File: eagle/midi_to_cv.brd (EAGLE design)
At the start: 100 x 80 mm, 57 parts, among them IC1 TL084P, IC2 TL084P, U1 ATMEGA328P_PDIP

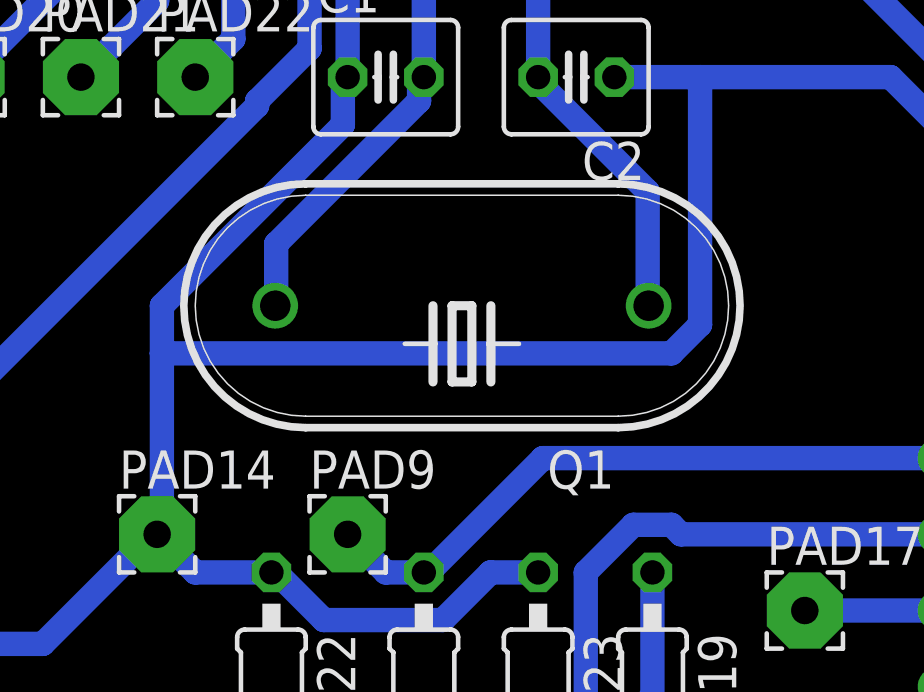
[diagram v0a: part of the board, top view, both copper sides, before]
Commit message: corrected to smaller xtal package
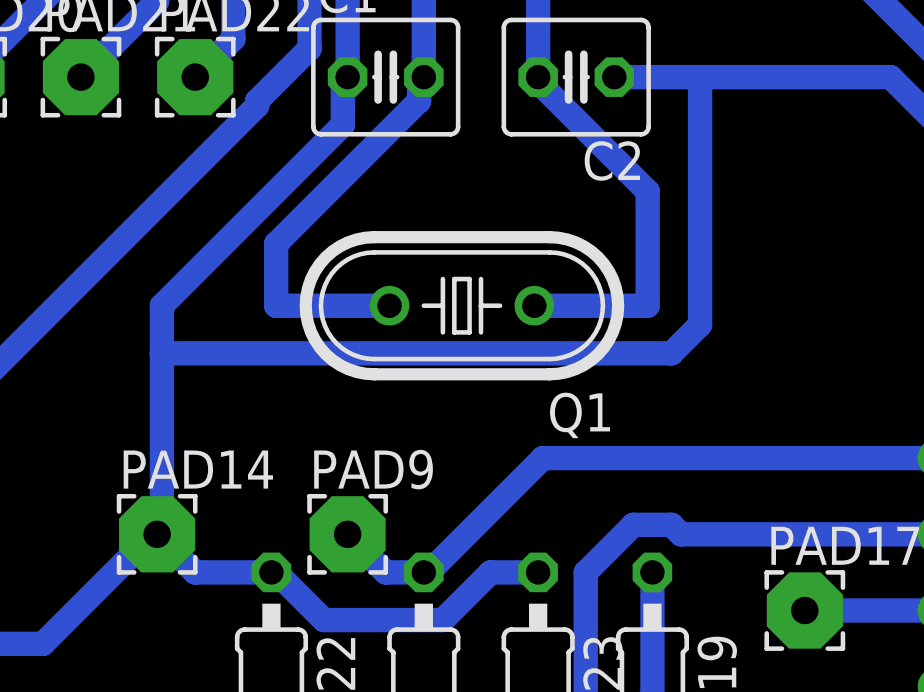
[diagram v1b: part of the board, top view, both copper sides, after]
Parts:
- Q1: device crystal:HC33U-V -> crystal:HC49U-V
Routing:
- net N$4: track 15.3 -> 19.0 mm
- net N$5: track 14.2 -> 18.0 mm
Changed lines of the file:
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@@
 <element name="C1" library="rcl" package="C025-040X050" value="27pF" x="38.1" y="38.1"/>
 <element name="C2" library="rcl" package="C025-040X050" value="27pF" x="44.45" y="38.1" rot="R180"/>
-<element name="Q1" library="crystal" package="HC33U-V" value="" x="40.64" y="30.48" rot="R180">
+<element name="Q1" library="crystal" package="HC49U-V" value="" x="40.64" y="30.48" rot="R180">
 <attribute name="OC_NEWARK" value="unknown" x="40.64" y="30.48" size="1.778" layer="27" rot="R180" display="off"/>
 <attribute name="MPN" value="" x="40.64" y="30.48" size="1.778" layer="27" rot="R180" display="off"/>
 <attribute name="MF" value="" x="40.64" y="30.48" size="1.778" layer="27" rot="R180" display="off"/>
-<attribute name="OC_FARNELL" value="unknown" x="40.64" y="30.48" size="1.778" layer="27" rot="R180" display="off"/>
+<attribute name="OC_FARNELL" value="1666969" x="40.64" y="30.48" size="1.778" layer="27" rot="R180" display="off"/>
 </element>
 <element name="U$1" library="eurorack" package="POWER_16" value="POWER" x="15.24" y="17.78" rot="R90"/>
@@
 <wire x1="39.21125" y1="37.30625" x2="34.44875" y2="32.54375" width="0.8128" layer="16"/>
 <wire x1="39.21125" y1="37.7825" x2="39.21125" y2="37.30625" width="0.8128" layer="16"/>
-<wire x1="34.44875" y1="30.48" x2="34.417" y2="30.48" width="0.8128" layer="16"/>
+<wire x1="34.44875" y1="30.48" x2="38.227" y2="30.48" width="0.8128" layer="16"/>
 <wire x1="39.21125" y1="37.7825" x2="39.37" y2="38.1" width="0.8128" layer="16"/>
 </signal>
@@
 <wire x1="46.83125" y1="34.29" x2="46.83125" y2="30.48" width="0.8128" layer="16"/>
 <wire x1="43.33875" y1="37.7825" x2="46.83125" y2="34.29" width="0.8128" layer="16"/>
-<wire x1="46.83125" y1="30.48" x2="46.863" y2="30.48" width="0.8128" layer="16"/>
+<wire x1="46.83125" y1="30.48" x2="43.053" y2="30.48" width="0.8128" layer="16"/>
 <wire x1="43.33875" y1="37.7825" x2="43.18" y2="38.1" width="0.8128" layer="16"/>
 </signal>
